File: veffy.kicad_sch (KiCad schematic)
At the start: 78 parts, among them J1 SWD, Q1 2N7002, Q2 BFR93A, Q3 2N7002, SW1 SW_Push, U1 ATSAMD21G18A-A, U2 ADF4112BCPZ, U3 SA612AN/01_112, U4 MC3361, U5 LM386, U6 LM358_DFN, U7 AD9834, Y2 TCXO-14

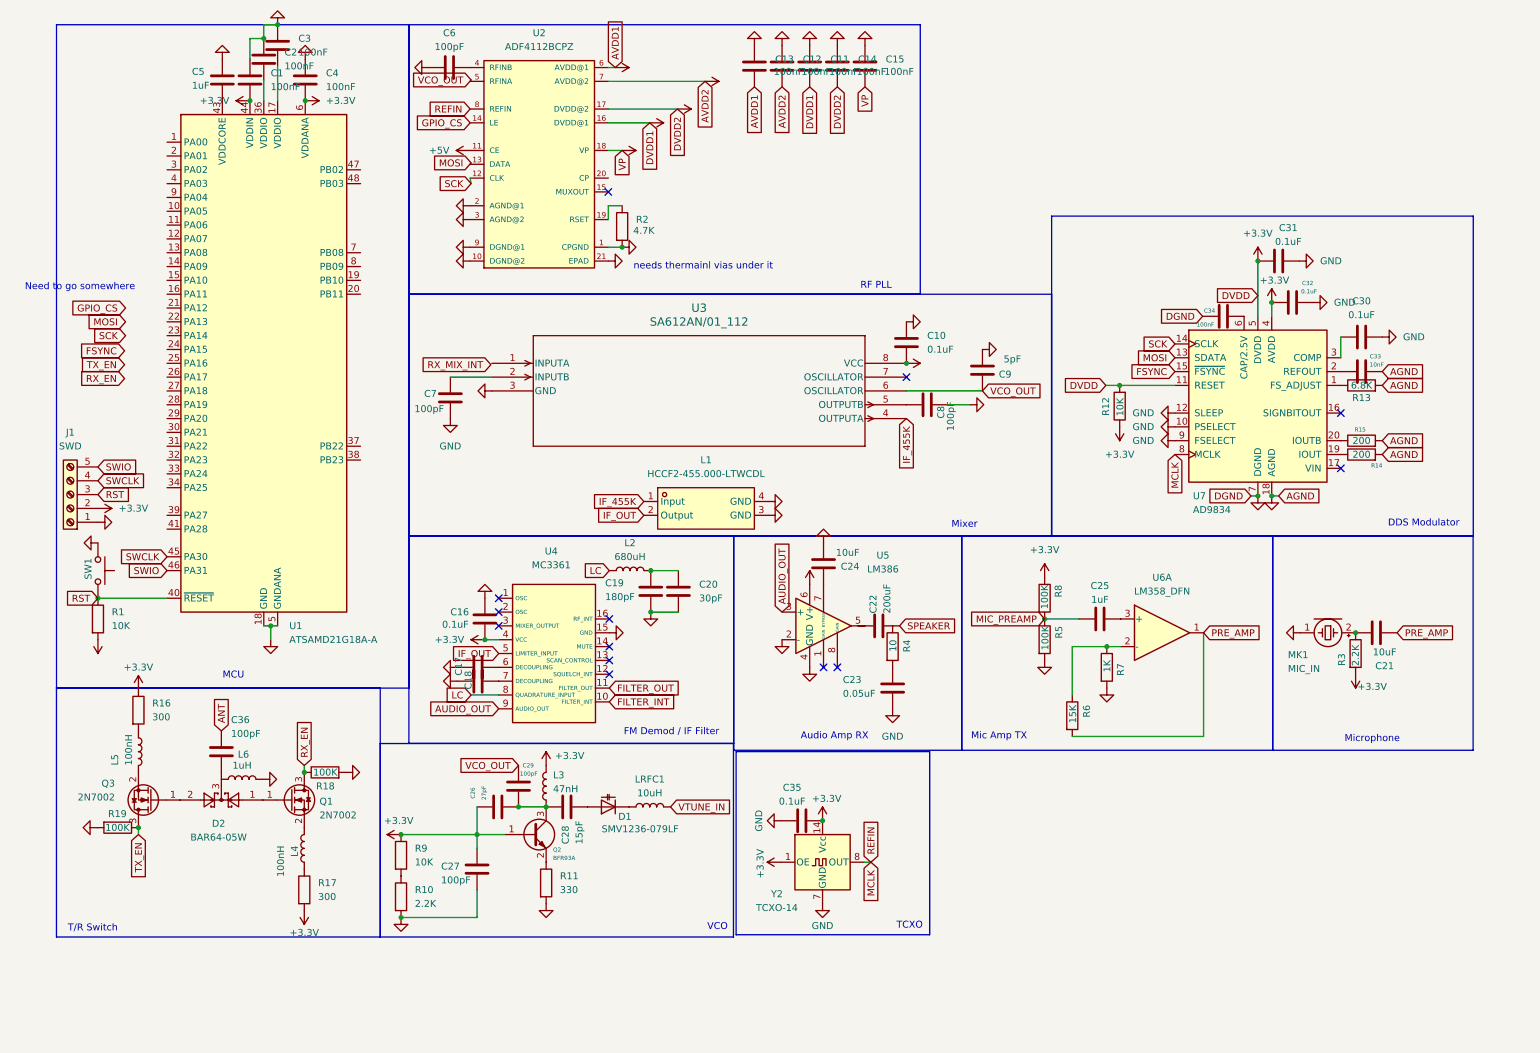
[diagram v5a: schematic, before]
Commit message: TX driver done
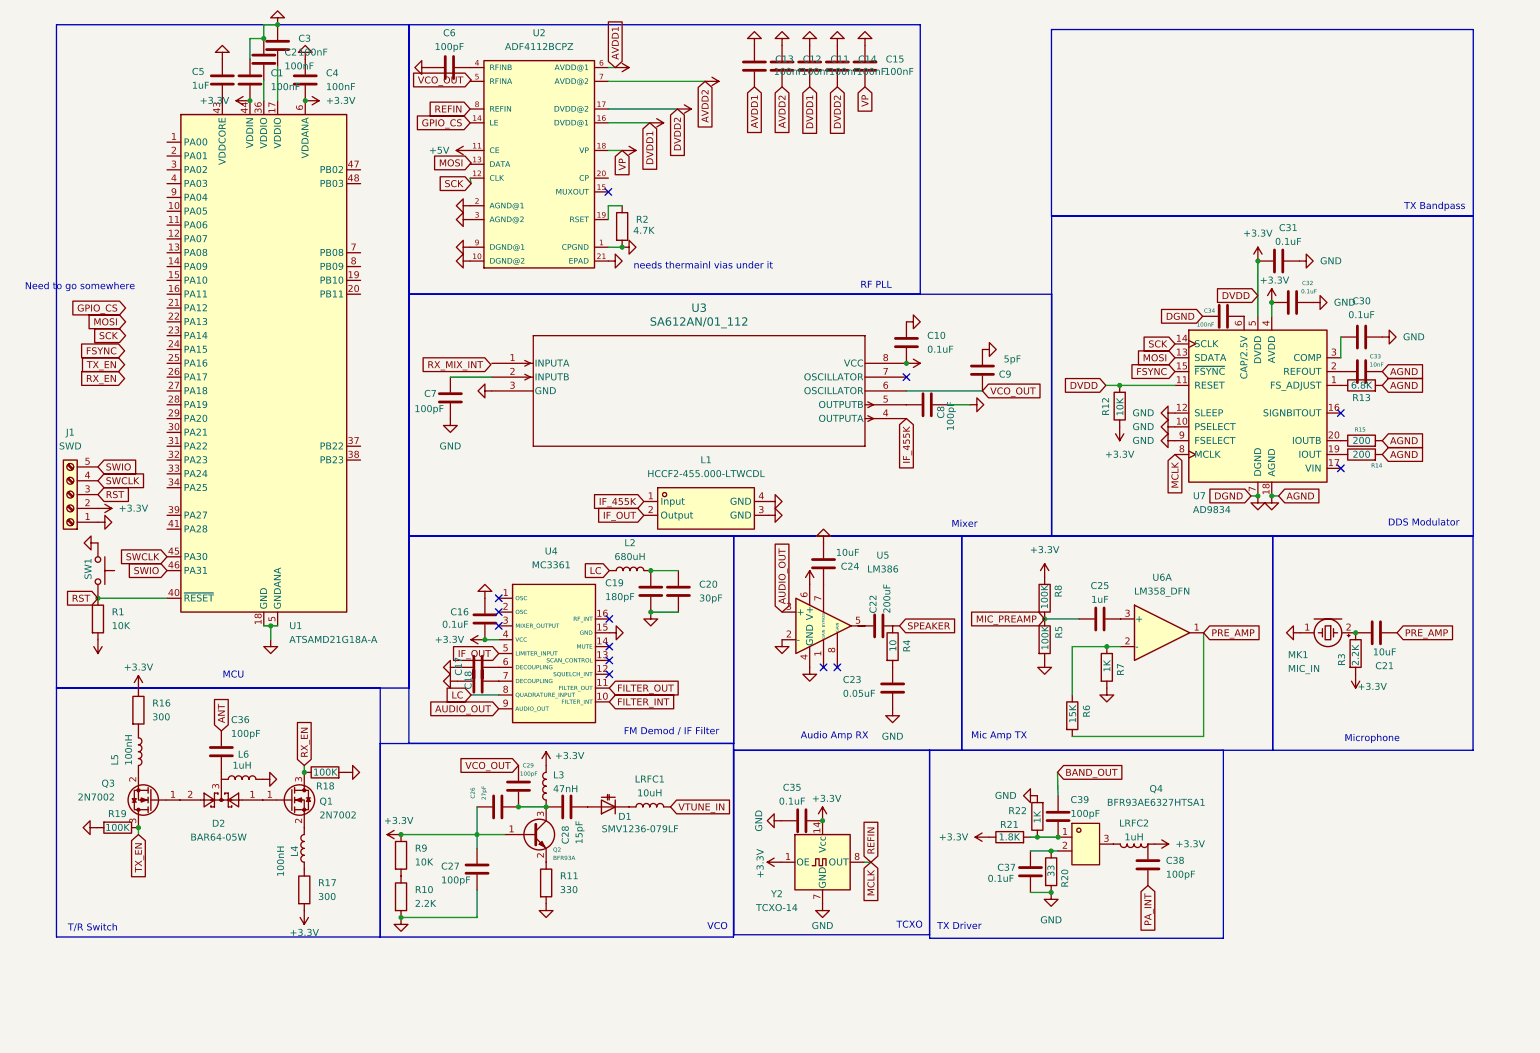
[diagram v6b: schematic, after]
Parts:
- added C37: 0.1uF, symbol Device:C
- added C38, C39: 100pF, symbol Device:C
- added LRFC2: 1uH, symbol Device:L
- added Q4: BFR93AE6327HTSA1, easyeda2kicad:SOT-23-3_L2.9-W1.3-P1.90-LS2.4-BR, symbol Easyeda2Kicad:BFR93AE6327HTSA1
- added R20: 33, symbol Device:R
- added R21: 1.8K, symbol Device:R
- added R22: 1K, symbol Device:R
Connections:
- net +3.3V: now also LRFC2.1, R21.1
- net GND: now also C37.2, R20.2, R22.2
- new net: C39.2, Q4.1, R21.2, R22.1
- new net: C37.1, Q4.2, R20.1
- new net: LRFC2.2, Q4.3
- new net BAND_OUT: C39.1
- new net PA_INT: C38.2
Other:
- note added: "TX Bandpass"
- note added: "TX Driver"

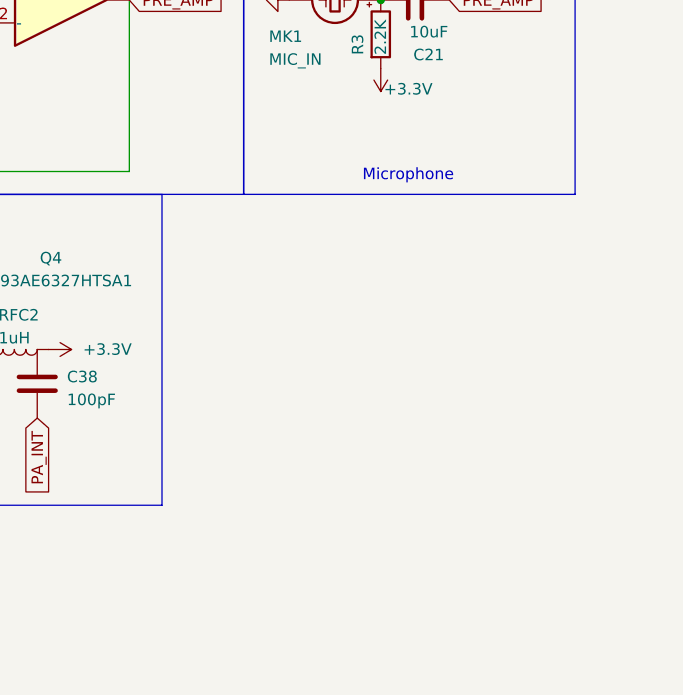
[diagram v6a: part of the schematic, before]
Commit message: started on the TX Power Amp and imported some parts into the PCB
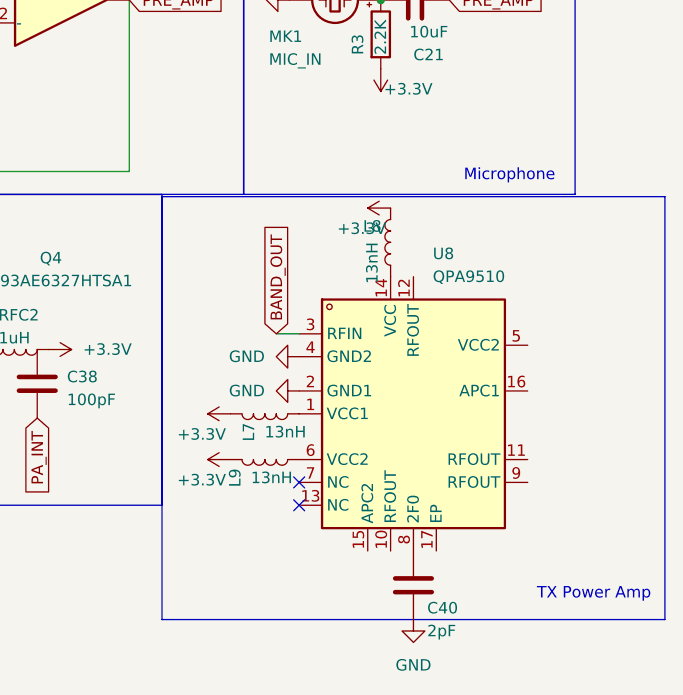
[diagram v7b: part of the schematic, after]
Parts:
- added C40: 2pF, Capacitor_SMD:C_0603_1608Metric, symbol Device:C
- added L7, L8, L9: 13nH, Inductor_SMD:L_0603_1608Metric, symbol Device:L
- added U8: QPA9510, Package_DFN_QFN:WQFN-16-1EP_3x3mm_P0.5mm_EP1.6x1.6mm_ThermalVias, symbol Amplifier_Audio:TPA6132A2RTE
- C36, C37, C38, C39: footprint (none) -> Capacitor_SMD:C_0603_1608Metric
- L2, L3, L4, L5, L6: footprint (none) -> Inductor_SMD:L_0603_1608Metric
- Q4: footprint easyeda2kicad:SOT-23-3_L2.9-W1.3-P1.90-LS2.4-BR -> Package_TO_SOT_SMD:SOT-23-3
- R20, R21, R22: footprint (none) -> Resistor_SMD:R_0603_1608Metric_Pad0.98x0.95mm_HandSolder
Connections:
- net +3.3V: now also L7.2, L8.2, L9.2
- net BAND_OUT: now also U8.3 (RFIN)
- net GND: now also C40.2, U8.2 (GND1), U8.4 (GND2)
- new net: L7.1, U8.1 (VCC1)
- new net: L8.1, U8.14 (VCC)
- new net: L9.1, U8.6 (VCC2)
- new net: C40.1, U8.8 (2F0)
- no-connect marks 13 -> 15
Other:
- note added: "TX Power Amp"

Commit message: almost done the power amp
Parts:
- added C41: 100pF, Capacitor_SMD:C_0603_1608Metric, symbol Device:C
- added L10: 13nH, Inductor_SMD:L_0603_1608Metric, symbol Device:L
- added R23, R26: 1.8K, symbol Device:R
- added R24, R25: 10K, symbol Device:R
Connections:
- net +3.3V: now also L10.2, R23.2, R26.2
- net BAND_OUT: now also C41.1; no longer U8.3 (RFIN)
- net GND: now also U8.17 (EP), R24.1, R25.1
- net at U8.15 (APC2): now also R25.2, R26.1
- net at U8.16 (APC1): now also R23.1, R24.2
- net at U8.5 (VCC2): now also L10.1
- new net: C41.2, U8.3 (RFIN)
